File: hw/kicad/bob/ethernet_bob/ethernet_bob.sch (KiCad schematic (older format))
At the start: 0 parts

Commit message: Add CS
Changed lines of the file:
@@
 F15 "STM_SPI1MISO" I L 6100 3650 60
 F16 "STM_SPI1SCK" I L 6100 3450 60
+F17 "STM_CS" I L 6100 3350 60
 $EndSheet
 Wire Wire Line
@@
 F1 "rs485.sch" 60
 $EndSheet
+Wire Wire Line
+	5400 3350 6100 3350
 $EndSCHEMATC

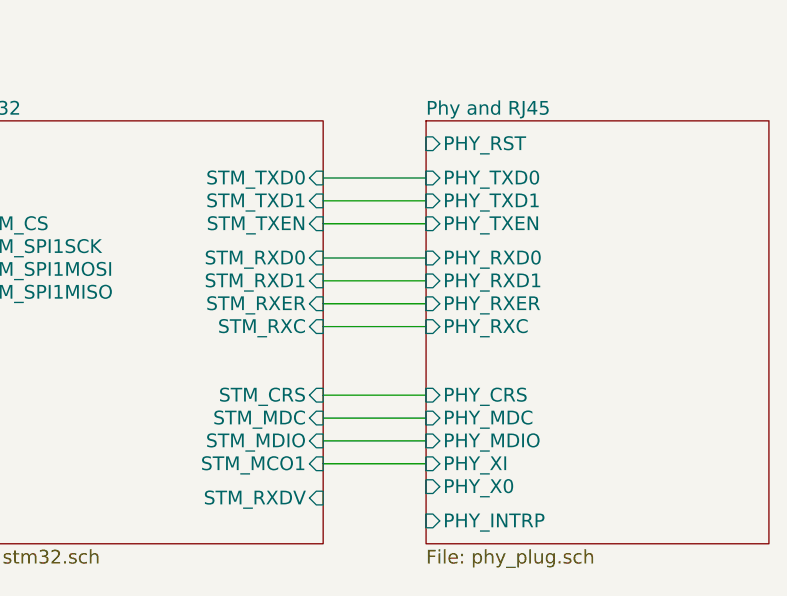
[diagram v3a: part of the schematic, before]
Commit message: add secondary crystal and hopefully connect magjack correctly?
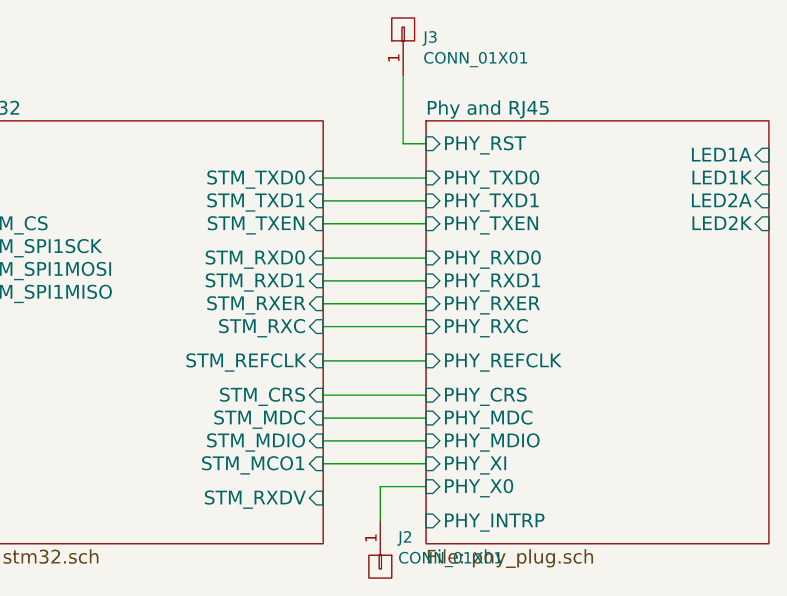
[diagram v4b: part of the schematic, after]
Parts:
- added J2, J3: CONN_01X01, Measurement_Points:Measurement_Point_Round-SMD-Pad_Big, symbol CONN_01X01
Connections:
- net Phy and RJ45/PHY_RST: now also J3.1 (P1)
- net Phy and RJ45/PHY_X0: now also J2.1 (P1)
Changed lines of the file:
@@
 EESchema Schematic File Version 2
+LIBS:ethernet_bob-rescue
 LIBS:power
 LIBS:device
@@
 Comment4 ""
 $EndDescr
-Wire Wire Line
-	7700 3150 8150 3150
-Wire Wire Line
-	7700 3250 8150 3250
-Wire Wire Line
-	7700 3350 8150 3350
-Wire Wire Line
-	7700 3500 8150 3500
-Wire Wire Line
-	7700 3600 8150 3600
 $Sheet
 S 8150 2900 1500 1850
@@
 F14 "PHY_INTRP" I L 8150 4650 60
 F15 "PHY_RXC" I L 8150 3800 60
+F16 "LED1A" I R 9650 3050 60
+F17 "LED1K" I R 9650 3150 60
+F18 "LED2A" I R 9650 3250 60
+F19 "LED2K" I R 9650 3350 60
+F20 "PHY_REFCLK" I L 8150 3950 60
 $EndSheet
-Wire Wire Line
-	7700 3800 8150 3800
-Wire Wire Line
-	7700 4100 8150 4100
-Wire Wire Line
-	7700 4200 8150 4200
-Wire Wire Line
-	7700 4300 8150 4300
-Wire Wire Line
-	7700 4400 8150 4400
-Wire Wire Line
-	7700 3700 8150 3700
 $Sheet
 S 4300 3900 1000 150
@@
 F16 "STM_SPI1SCK" I L 6100 3450 60
 F17 "STM_CS" I L 6100 3350 60
+F18 "STM_REFCLK" I R 7700 3950 60
 $EndSheet
+$Sheet
+S 4300 4300 1000 400
+U 58076FA4
+F0 "rs485" 60
+F1 "rs485.sch" 60
+$EndSheet
+$Comp
+L CONN_01X01 J3
+U 1 1 59A7C874
+P 8050 2500
+F 0 "J3" V 8015 2412 50  0000 R CNN
+F 1 "CONN_01X01" V 7924 2412 50  0000 R CNN
+F 2 "Measurement_Points:Measurement_Point_Round-SMD-Pad_Big" H 8050 2500 50  0001 C CNN
+F 3 "" H 8050 2500 50  0001 C CNN
+	1    8050 2500
+	0    -1   -1   0
+$EndComp
+$Comp
+L CONN_01X01 J2
+U 1 1 59A81F51
+P 7950 4850
+F 0 "J2" V 7822 4928 50  0000 L CNN
+F 1 "CONN_01X01" V 7913 4928 50  0000 L CNN
+F 2 "Measurement_Points:Measurement_Point_Round-SMD-Pad_Big" H 7950 4850 50  0001 C CNN
+F 3 "" H 7950 4850 50  0001 C CNN
+	1    7950 4850
+	0    1    1    0
+$EndComp
+Wire Wire Line
+	7700 3150 8150 3150
+Wire Wire Line
+	7700 3250 8150 3250
+Wire Wire Line
+	7700 3350 8150 3350
+Wire Wire Line
+	7700 3500 8150 3500
+Wire Wire Line
+	7700 3600 8150 3600
+Wire Wire Line
+	7700 3800 8150 3800
+Wire Wire Line
+	7700 4100 8150 4100
+Wire Wire Line
+	7700 4200 8150 4200
+Wire Wire Line
+	7700 4300 8150 4300
+Wire Wire Line
+	7700 4400 8150 4400
+Wire Wire Line
+	7700 3700 8150 3700
 Wire Wire Line
 	5400 3450 6100 3450
@@
 Wire Wire Line
 	5400 3650 6100 3650
-$Sheet
-S 4300 4300 1000 400
-U 58076FA4
-F0 "rs485" 60
-F1 "rs485.sch" 60
-$EndSheet
 Wire Wire Line
 	5400 3350 6100 3350
+Wire Wire Line
+	8050 2700 8050 3000
+Wire Wire Line
+	8050 3000 8150 3000
+Wire Wire Line
+	8150 4500 7950 4500
+Wire Wire Line
+	7950 4500 7950 4650
+Wire Wire Line
+	7700 3950 8150 3950
 $EndSCHEMATC

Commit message: Attached the second LED in the BOB. Schematic is probably horribly broken now until everybody migrates to the new library shipped by upstream Kicad. :/
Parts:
- J2, J3: symbol CONN_01X01 -> conn:CONN_01X01
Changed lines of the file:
@@
-EESchema Schematic File Version 2
-LIBS:ethernet_bob-rescue
-LIBS:power
-LIBS:device
-LIBS:transistors
-LIBS:conn
-LIBS:linear
-LIBS:regul
-LIBS:74xx
-LIBS:cmos4000
-LIBS:adc-dac
-LIBS:memory
-LIBS:xilinx
-LIBS:microcontrollers
-LIBS:dsp
-LIBS:microchip
-LIBS:analog_switches
-LIBS:motorola
-LIBS:texas
-LIBS:intel
-LIBS:audio
-LIBS:interface
-LIBS:digital-audio
-LIBS:philips
-LIBS:display
-LIBS:cypress
-LIBS:siliconi
-LIBS:opto
-LIBS:atmel
-LIBS:contrib
-LIBS:valves
-LIBS:ksz8081
-LIBS:ESD_Protection
-LIBS:hr911105_rj45
-LIBS:stm32
-LIBS:crystal_smd
-LIBS:usblc
+EESchema Schematic File Version 4
 LIBS:ethernet_bob-cache
 EELAYER 26 0
@@
 $EndSheet
 $Comp
-L CONN_01X01 J3
+L conn:CONN_01X01 J3
 U 1 1 59A7C874
 P 8050 2500
@@
 $EndComp
 $Comp
-L CONN_01X01 J2
+L conn:CONN_01X01 J2
 U 1 1 59A81F51
 P 7950 4850
@@
 Wire Wire Line
 	7700 3950 8150 3950
+Text GLabel 9750 3350 2    60   Input ~ 0
+LED2
+Wire Wire Line
+	9650 3350 9750 3350
 $EndSCHEMATC

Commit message: change to single crystal
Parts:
- J2, J3: symbol conn:CONN_01X01 -> Connector:Conn_01x01
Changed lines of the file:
@@
 $EndSheet
 $Comp
-L conn:CONN_01X01 J3
+L Connector:Conn_01x01 J3
 U 1 1 59A7C874
 P 8050 2500
@@
 $EndComp
 $Comp
-L conn:CONN_01X01 J2
+L Connector:Conn_01x01 J2
 U 1 1 59A81F51
 P 7950 4850

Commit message: change over to 4 layer, change cpu to F7
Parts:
- J2, J3: symbol Connector:Conn_01x01 -> stmbl:CONN_01X01
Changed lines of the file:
@@
 EESchema Schematic File Version 4
 LIBS:ethernet_bob-cache
-EELAYER 26 0
+EELAYER 29 0
 EELAYER END
 $Descr A4 11693 8268
@@
 Comment4 ""
 $EndDescr
-$Sheet
-S 8150 2900 1500 1850
-U 57A86254
-F0 "Phy and RJ45" 60
-F1 "phy_plug.sch" 60
-F2 "PHY_RST" I L 8150 3000 60
-F3 "PHY_CRS" I L 8150 4100 60
-F4 "PHY_TXD1" I L 8150 3250 60
-F5 "PHY_TXD0" I L 8150 3150 60
-F6 "PHY_TXEN" I L 8150 3350 60
-F7 "PHY_RXER" I L 8150 3700 60
-F8 "PHY_RXD0" I L 8150 3500 60
-F9 "PHY_RXD1" I L 8150 3600 60
-F10 "PHY_MDC" I L 8150 4200 60
-F11 "PHY_MDIO" I L 8150 4300 60
-F12 "PHY_XI" I L 8150 4400 60
-F13 "PHY_X0" I L 8150 4500 60
-F14 "PHY_INTRP" I L 8150 4650 60
-F15 "PHY_RXC" I L 8150 3800 60
-F16 "LED1A" I R 9650 3050 60
-F17 "LED1K" I R 9650 3150 60
-F18 "LED2A" I R 9650 3250 60
-F19 "LED2K" I R 9650 3350 60
-F20 "PHY_REFCLK" I L 8150 3950 60
-$EndSheet
 $Sheet
 S 4300 3900 1000 150
@@
 $EndSheet
 $Comp
-L Connector:Conn_01x01 J3
+L stmbl:CONN_01X01 J3
 U 1 1 59A7C874
 P 8050 2500
@@
 $EndComp
 $Comp
-L Connector:Conn_01x01 J2
+L stmbl:CONN_01X01 J2
 U 1 1 59A81F51
 P 7950 4850
@@
 Wire Wire Line
 	9650 3350 9750 3350
+$Sheet
+S 8150 2900 1500 1850
+U 57A86254
+F0 "Phy and RJ45" 60
+F1 "phy_plug.sch" 60
+F2 "PHY_RST" I L 8150 3000 60
+F3 "PHY_CRS" I L 8150 4100 60
+F4 "PHY_TXD1" I L 8150 3250 60
+F5 "PHY_TXD0" I L 8150 3150 60
+F6 "PHY_TXEN" I L 8150 3350 60
+F7 "PHY_RXER" I L 8150 3700 60
+F8 "PHY_RXD0" I L 8150 3500 60
+F9 "PHY_RXD1" I L 8150 3600 60
+F10 "PHY_MDC" I L 8150 4200 60
+F11 "PHY_MDIO" I L 8150 4300 60
+F12 "PHY_XI" I L 8150 4400 60
+F13 "PHY_X0" I L 8150 4500 60
+F14 "PHY_INTRP" I L 8150 4650 60
+F15 "PHY_RXC" I L 8150 3800 60
+F16 "LED1A" I R 9650 3050 60
+F17 "LED1K" I R 9650 3150 60
+F18 "LED2A" I R 9650 3250 60
+F19 "LED2K" I R 9650 3350 60
+F20 "PHY_REFCLK" I L 8150 3950 60
+$EndSheet
 $EndSCHEMATC
